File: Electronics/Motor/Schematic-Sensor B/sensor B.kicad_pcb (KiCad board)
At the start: 2 copper layers, 12 x 23 mm, 3 parts, among them J1 CONN_01X06, U1 MA700

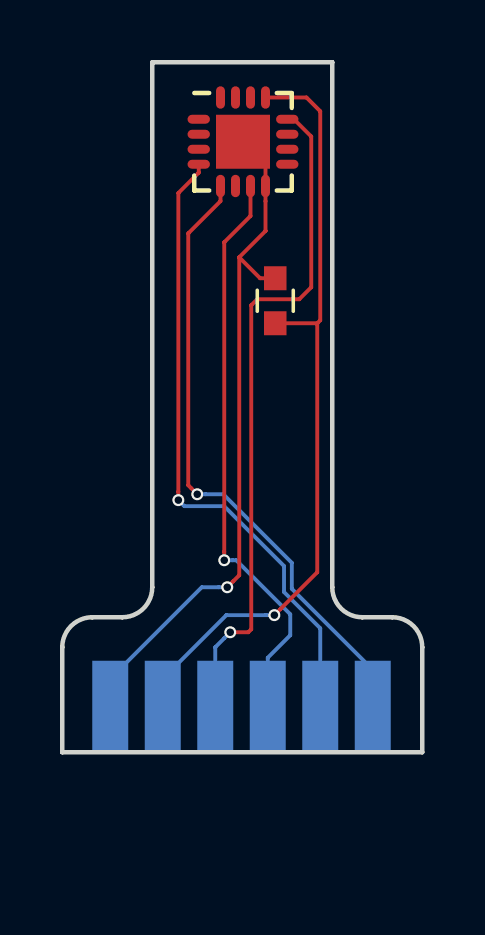
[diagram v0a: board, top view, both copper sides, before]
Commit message: motor 8 fixes; sensor flex PCB correction.
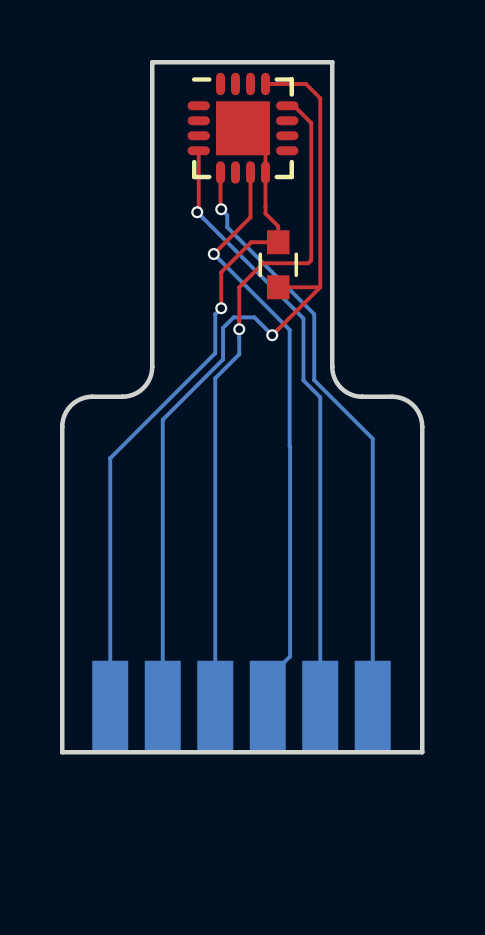
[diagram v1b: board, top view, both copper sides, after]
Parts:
- moved C1 1.20 mm to (94.2, 66.8)
- moved U1 0.45 mm to (93.0, 62.2)
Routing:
- net +3V3: track 26.3 -> 27.4 mm
- net CS: track 20.8 -> 19.9 mm
- net MOSI: track 21.1 -> 20.2 mm
- net Earth: track 25.3 -> 24.6 mm
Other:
- outline, holes or cut-outs redrawn

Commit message: gyro is working
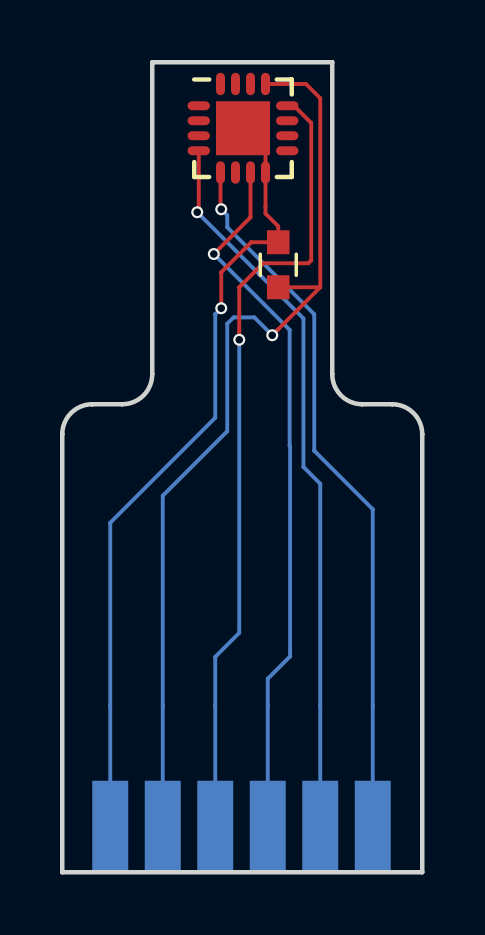
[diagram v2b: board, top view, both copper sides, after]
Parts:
- moved J1 4.00 mm to (95.7, 82.7)
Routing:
- net SCLK: track 22.7 -> 26.7 mm
- net MOSI: track 20.2 -> 24.2 mm
- net MISO: track 19.6 -> 23.6 mm
- net Earth: track 24.6 -> 28.6 mm
- net CS: track 19.9 -> 23.9 mm
- net +3V3: track 27.4 -> 31.4 mm
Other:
- board size 12 x 23 mm -> 12 x 27 mm
